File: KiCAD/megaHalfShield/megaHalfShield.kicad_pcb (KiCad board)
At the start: 2 copper layers, 35.1 x 53.3 mm, 9 parts, among them J1 Conn_02x05_Odd_Even, J2 Conn_01x01, P1 Digital, P10 CONN_01X01, P13 CONN_01X01, P4 Analog, P7 Communication

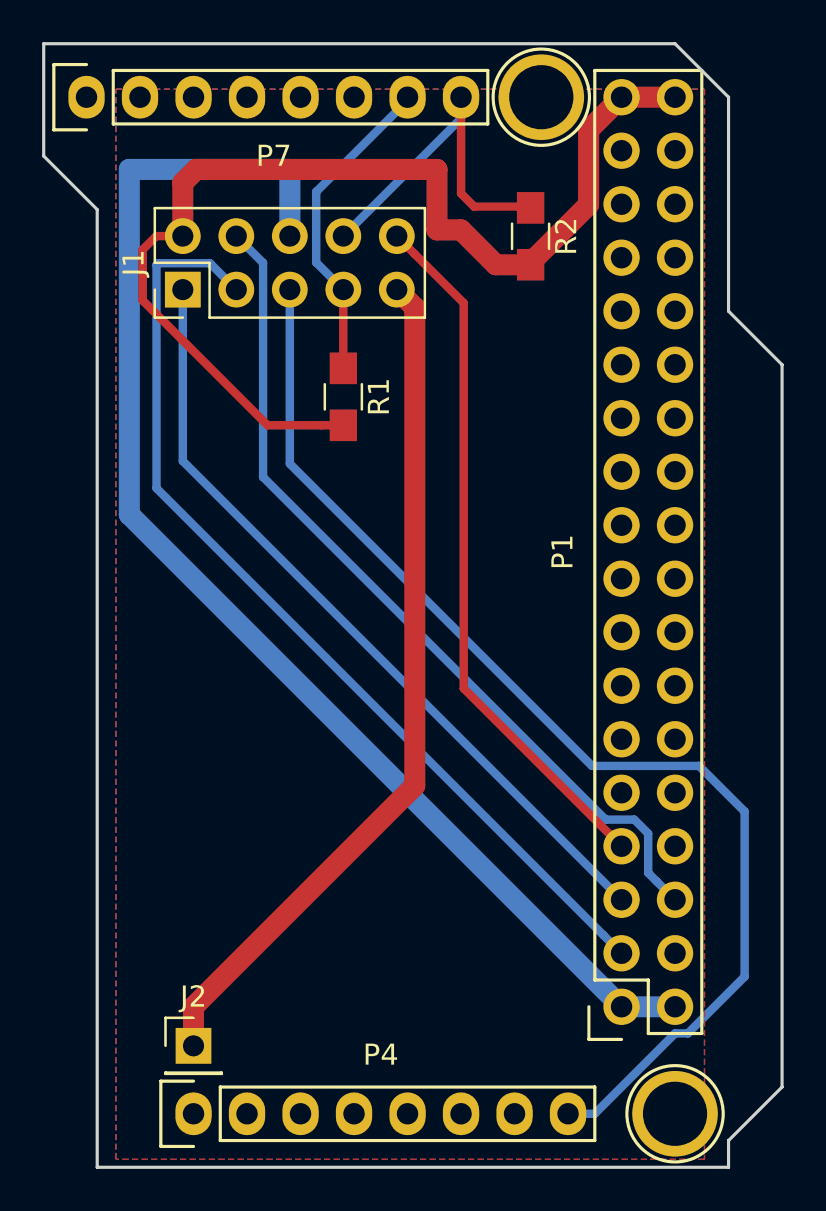
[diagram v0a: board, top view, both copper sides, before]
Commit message: move arduino headers into myparts
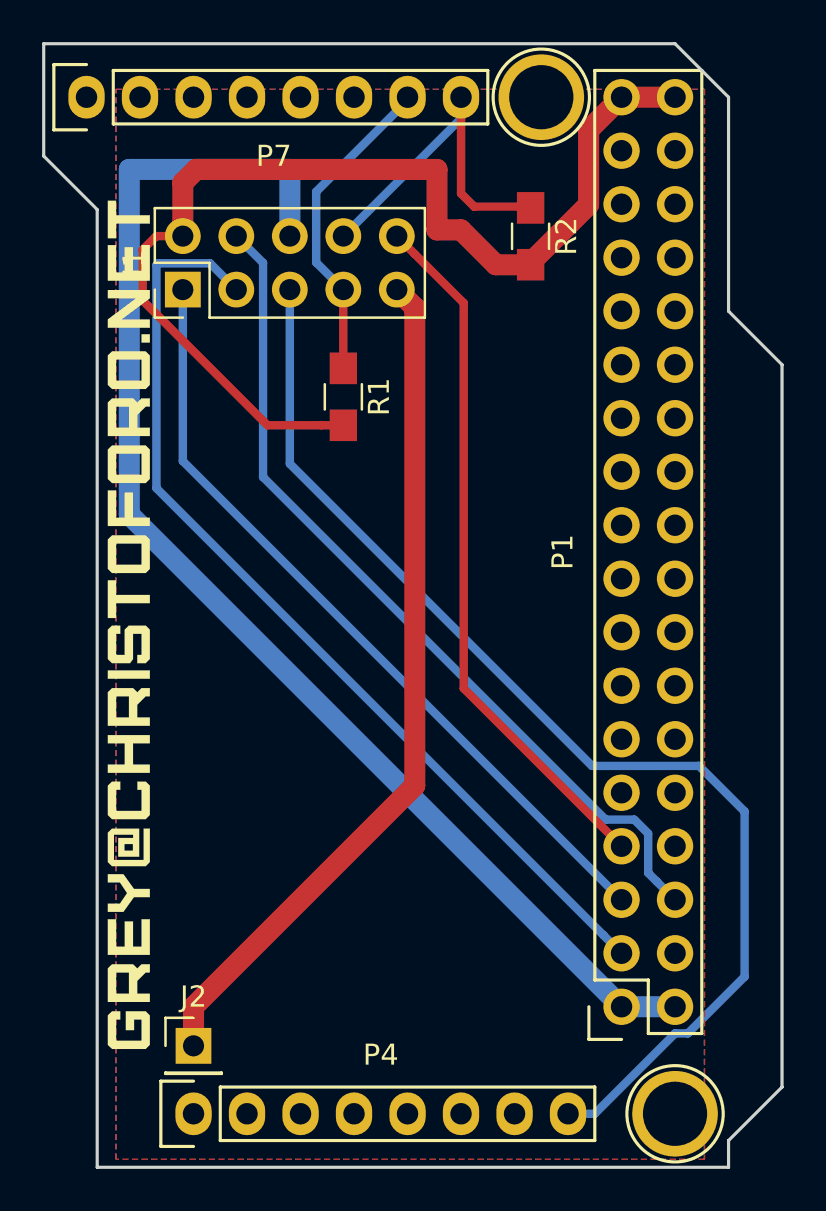
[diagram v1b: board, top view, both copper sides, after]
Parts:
- added L1: GREY@CHRISTOFORO.NET, myparts:logo, F.Cu at (174.0, 95.9)
- P1: footprint Socket_Arduino_Mega:Socket_Strip_Arduino_2x18 -> myparts:Socket_Strip_Arduino_2x18
- P10, P13: footprint Socket_Arduino_Mega:Arduino_1pin -> myparts:Arduino_1pin
- P4, P7: footprint Socket_Arduino_Mega:Socket_Strip_Arduino_1x08 -> myparts:Socket_Strip_Arduino_1x08

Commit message: update silk
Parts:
- moved L1 4.44 mm to (174.0, 100.3)
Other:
- board text added: "3ec2e93"
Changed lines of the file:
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@@
   (general
     (thickness 1.6)
-    (drawings 11)
+    (drawings 12)
     (tracks 66)
     (zones 0)
@@
     (visible_elements FFFFFF7F)
     (pcbplotparams
-      (layerselection 0x00030_80000001)
+      (layerselection 0x010fc_ffffffff)
       (usegerberextensions false)
       (usegerberattributes true)
@@
       (outputformat 1)
       (mirror false)
-      (drillshape 1)
+      (drillshape 0)
       (scaleselection 1)
-      (outputdirectory ""))
+      (outputdirectory output/))
   )
   (net 0 "")
@@
   )
   (module myparts:logo (layer F.Cu)
-    (at 173.99 95.885 90)
+    (at 173.99 100.33 90)
     (fp_text reference L1 (at 0 -4 90) (layer F.SilkS) hide
       (effects (font (size 1.524 1.524) (thickness 0.2)))
@@
     (pad 1 thru_hole circle (at 0 0) (size 4.064 4.064) (drill 3.048) (layers *.Cu *.Mask F.SilkS))
   )
+  (gr_text 3ec2e93 (at 176.53 86.36 90) (layer F.SilkS)
+    (effects (font (size 1.5 1.5) (thickness 0.3)))
+  )
   (gr_line (start 172.466 76.2) (end 169.926 73.66) (layer Edge.Cuts) (width 0.15))

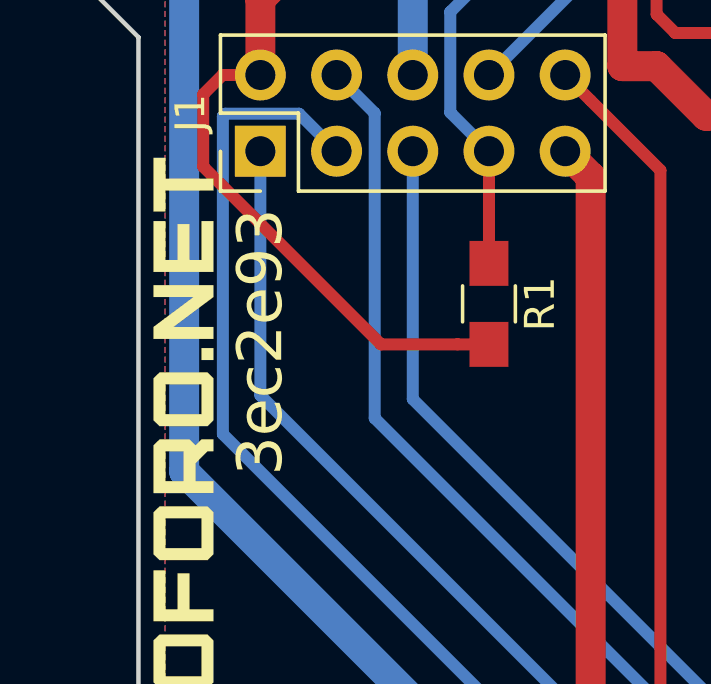
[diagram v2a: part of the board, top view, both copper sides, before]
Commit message: starting on ethercat board pin boards rotated base1x zones fixed
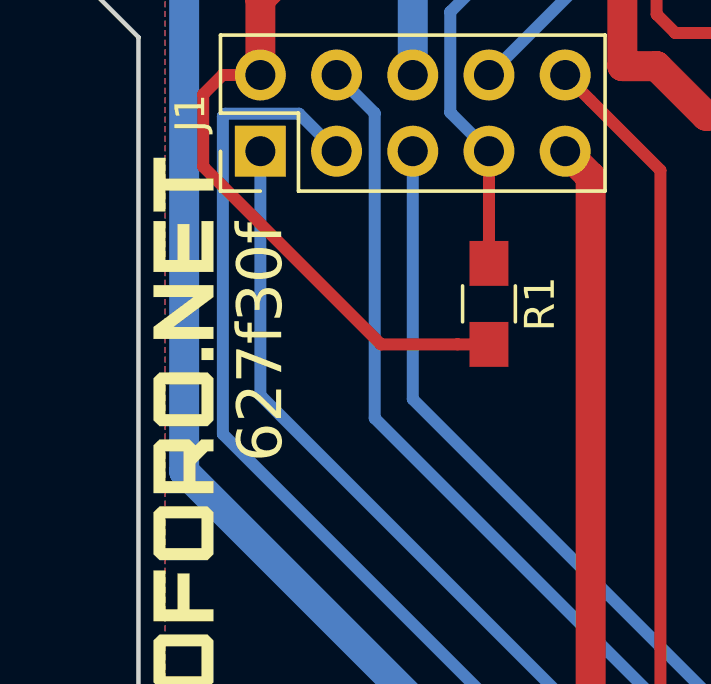
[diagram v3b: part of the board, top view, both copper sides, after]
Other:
- board text added: "627f30f"
- board text removed: "3ec2e93"
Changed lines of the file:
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@@
-(kicad_pcb (version 20171130) (host pcbnew "(5.0-dev-4060-g28f1209ce)")
+(kicad_pcb (version 20171130) (host pcbnew "(5.0-dev-4085-g9241a399a)")
   (general
     (thickness 1.6)
@@
     (pcbplotparams
       (layerselection 0x010fc_ffffffff)
-      (usegerberextensions false)
+      (usegerberextensions true)
       (usegerberattributes true)
       (usegerberadvancedattributes true)
@@
     (pad 1 thru_hole circle (at 0 0) (size 4.064 4.064) (drill 3.048) (layers *.Cu *.Mask F.SilkS))
   )
-  (gr_text 3ec2e93 (at 176.53 86.36 90) (layer F.SilkS)
+  (gr_text 627f30f (at 176.53 86.36 90) (layer F.SilkS)
     (effects (font (size 1.5 1.5) (thickness 0.3)))
   )

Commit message: update silk
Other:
- board text added: "20b2bb8"
- board text removed: "627f30f"
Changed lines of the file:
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@@
-(kicad_pcb (version 20171130) (host pcbnew "(5.0-dev-4085-g9241a399a)")
+(kicad_pcb (version 20171130) (host pcbnew "(5.0.0-rc2-dev-44-gde6b32d23)")
   (general
     (thickness 1.6)
@@
       (usegerberattributes true)
       (usegerberadvancedattributes true)
-      (creategerberjobfile true)
+      (creategerberjobfile false)
       (excludeedgelayer true)
       (linewidth 0.100000)
@@
     (pad 1 thru_hole circle (at 0 0) (size 4.064 4.064) (drill 3.048) (layers *.Cu *.Mask F.SilkS))
   )
-  (gr_text 627f30f (at 176.53 86.36 90) (layer F.SilkS)
+  (gr_text 20b2bb8 (at 176.53 86.36 90) (layer F.SilkS)
     (effects (font (size 1.5 1.5) (thickness 0.3)))
   )
